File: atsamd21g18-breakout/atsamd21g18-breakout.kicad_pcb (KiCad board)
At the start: 2 copper layers, 48.1 x 36.8 mm, 28 parts, among them J1 SWD, J2 MICRO USB, J3 HEADER-FEMALE-18POS-TH-1x18-P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, J4 HEADER-FEMALE-18POS-TH-1x18-P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, U1 BU33SD5WG 500mA, U2 IC-MCU-ATSAMD21G18A-TQFP48-CU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, X1 16MHz

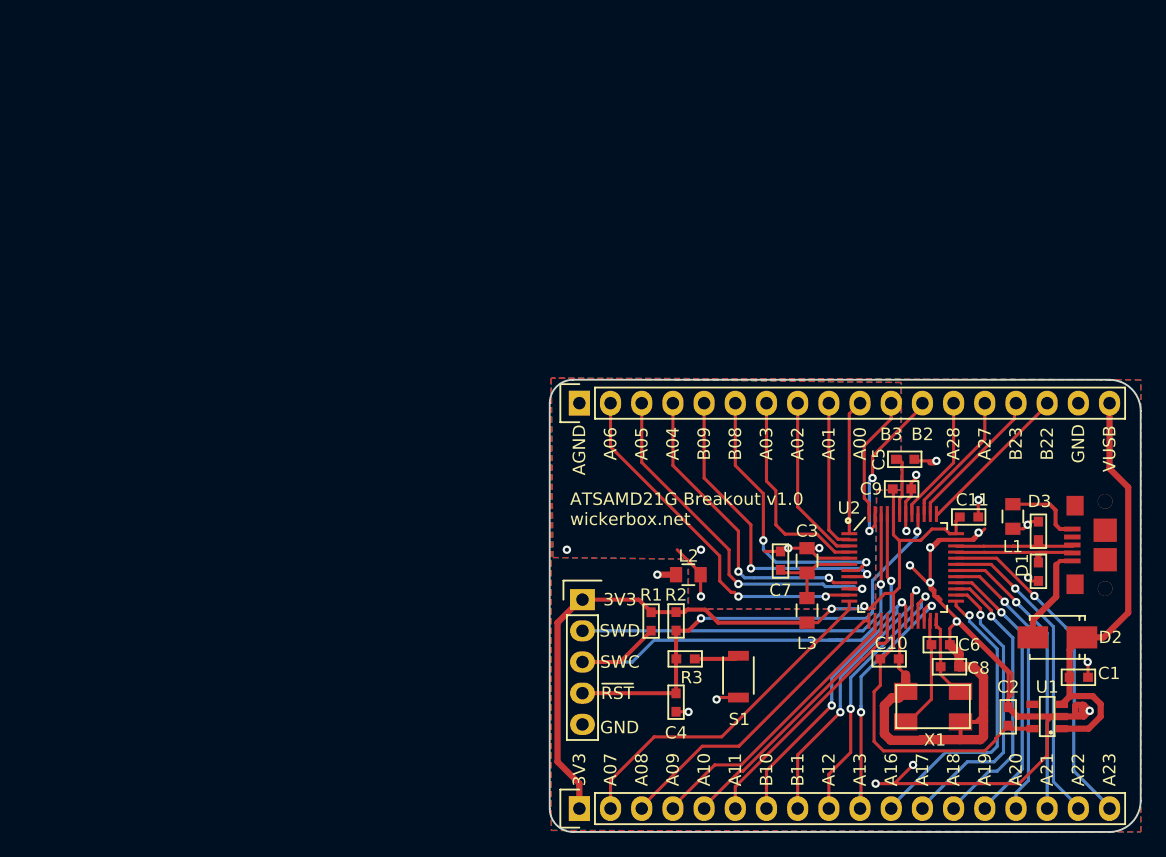
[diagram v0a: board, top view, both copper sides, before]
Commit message: Updating v1.0 with FabNotes file.
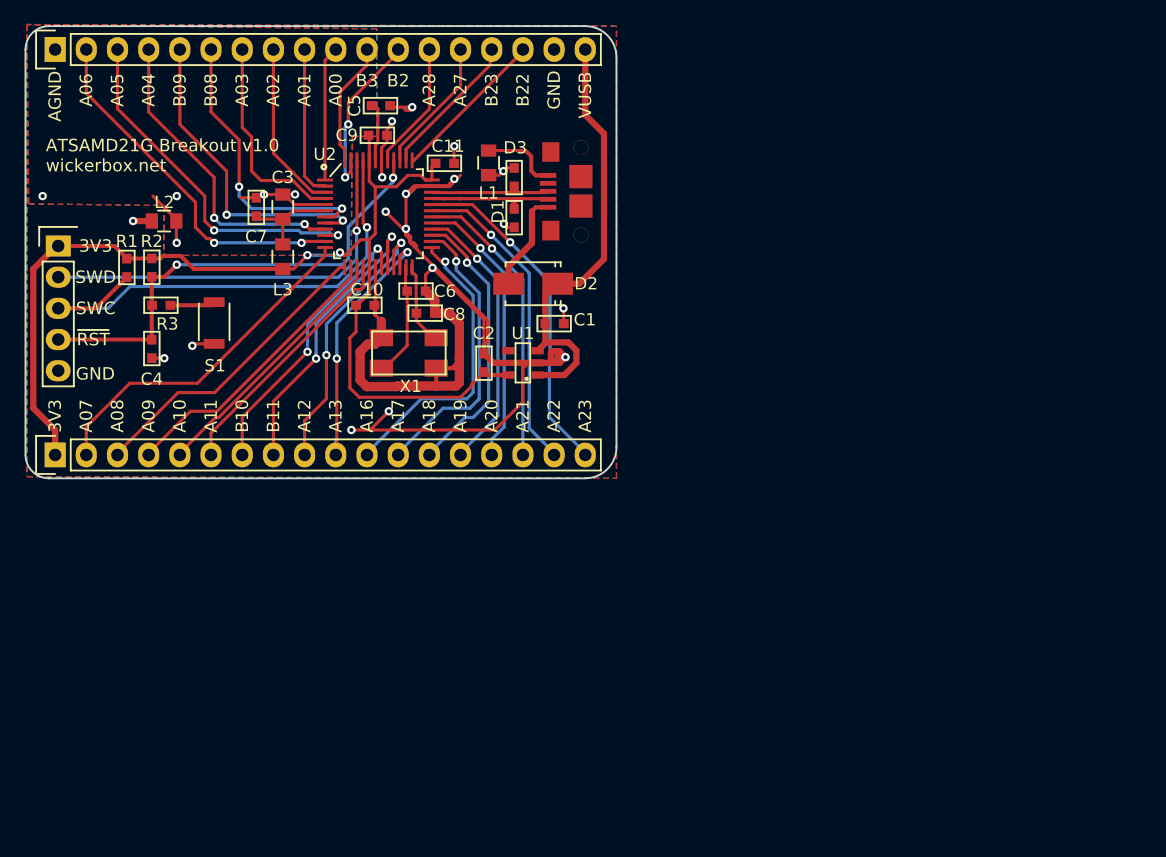
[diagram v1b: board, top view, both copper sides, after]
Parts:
- moved C1 51.5 mm to (62.8, 51.9)
- moved C10 51.5 mm to (47.3, 50.4)
- moved C4 51.5 mm to (29.9, 54.0)
- moved C6 51.5 mm to (51.5, 49.3)
- moved C7 51.5 mm to (38.5, 42.4)
- moved C8 51.5 mm to (52.2, 51.1)
- moved D1 51.5 mm to (59.5, 43.3)
- moved D2 51.5 mm to (61.0, 48.7)
- moved L2 51.5 mm to (30.9, 43.6)
- moved R2 51.5 mm to (29.9, 47.4)
- moved R3 51.5 mm to (30.7, 50.4)
- moved S1 51.5 mm to (35.0, 50.2)
- moved C11 51.5 mm to (53.8, 38.9)
- moved C2 51.5 mm to (57.0, 55.1)
- moved C5 51.5 mm to (48.6, 34.2)
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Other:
- board text added: "FABRICATION NOTES 1. THIS IS A 2 LAYER BOARD. 2. EXTERNAL LAYERS SHALL HAVE 1 OZ COPPER. 3. MATERIAL: FR4 AND 0.062 INCH +/- 10% THICK. 4. BOARDS SHALL BE ROHS COMPLIANT. 5. MANUFACTURE IN ACCORDANCE WITH IPC-6012 CLASS 2 6. MASK: BOTH SIDES OF THE BOARD SHALL HAVE SOLDER MASK (ANY COLOR) OVER BARE COPPER. 7. SILK: BOTH SIDES OF THE BOARD SHALL HAVE WHITE SILKSCREEN. DO NOT PLACE SILK OVER BARE C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"
